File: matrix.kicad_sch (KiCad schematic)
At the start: 189 parts

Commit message: Outline adjustment, footprint cleanup
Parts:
- Stab-225U1, Stab-225U2, Stab-225U3, Stab-275U1, Stab-2U1, Stab-625U1, Stab-7U1: symbol Connector_Generic:Conn_01x01 -> Mechanical:MountingHole
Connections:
- no-connect marks 7 -> 0
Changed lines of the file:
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@@
   (junction (at 261.62 203.2) (diameter 0) (color 0 0 0 0)
   )
-  (no_connect (at 231.14 262.89))
-  (no_connect (at 254 262.89))
-  (no_connect (at 208.28 262.89))
-  (no_connect (at 254 267.97))
-  (no_connect (at 231.14 267.97))
-  (no_connect (at 254 273.05))
-  (no_connect (at 208.28 267.97))
   (wire (pts (xy 307.34 146.05) (xy 307.34 144.78))
     (stroke (width 0) (type default) (color 0 0 0 0))
@@
     (pin "2")
   )
-  (symbol (lib_id "Connector_Generic:Conn_01x01") (at 213.36 262.89 0) (unit 1)
+  (symbol (lib_id "Mechanical:MountingHole") (at 213.36 262.89 0) (unit 1)
     (in_bom yes) (on_board yes)
     (property "Reference" "Stab-625U1" (id 0) (at 215.392 261.8232 0)
@@
       (effects (font (size 1.27 1.27)) hide)
     )
-    (pin "1")
   )
   (symbol (lib_id "MX_Alps_Hybrid:MX-NoLED") (at 97.79 97.79 0) (unit 1)
@@
     (pin "2")
   )
-  (symbol (lib_id "Connector_Generic:Conn_01x01") (at 213.36 267.97 0) (unit 1)
+  (symbol (lib_id "Mechanical:MountingHole") (at 213.36 267.97 0) (unit 1)
     (in_bom yes) (on_board yes)
     (property "Reference" "Stab-7U1" (id 0) (at 215.392 266.9032 0)
@@
       (effects (font (size 1.27 1.27)) hide)
     )
-    (pin "1")
   )
   (symbol (lib_id "MX_Alps_Hybrid:MX-NoLED") (at 229.87 135.89 0) (unit 1)
@@
     (pin "2")
   )
-  (symbol (lib_id "Connector_Generic:Conn_01x01") (at 236.22 267.97 0) (unit 1)
+  (symbol (lib_id "Mechanical:MountingHole") (at 236.22 267.97 0) (unit 1)
     (in_bom yes) (on_board yes)
     (property "Reference" "Stab-225U1" (id 0) (at 238.252 266.9032 0)
@@
       (effects (font (size 1.27 1.27)) hide)
     )
-    (pin "1")
   )
   (symbol (lib_id "MX_Alps_Hybrid:MX-NoLED") (at 163.83 173.99 0) (unit 1)
@@
     (pin "2")
   )
-  (symbol (lib_id "Connector_Generic:Conn_01x01") (at 236.22 262.89 0) (unit 1)
+  (symbol (lib_id "Mechanical:MountingHole") (at 236.22 262.89 0) (unit 1)
     (in_bom yes) (on_board yes)
     (property "Reference" "Stab-2U1" (id 0) (at 238.252 261.8232 0)
@@
       (effects (font (size 1.27 1.27)) hide)
     )
-    (pin "1")
   )
   (symbol (lib_id "MX_Alps_Hybrid:MX-NoLED") (at 97.79 199.39 0) (unit 1)
@@
     (pin "2")
   )
-  (symbol (lib_id "Connector_Generic:Conn_01x01") (at 259.08 267.97 0) (unit 1)
+  (symbol (lib_id "Mechanical:MountingHole") (at 259.08 267.97 0) (unit 1)
     (in_bom yes) (on_board yes)
     (property "Reference" "Stab-225U3" (id 0) (at 261.112 266.9032 0)
@@
       (effects (font (size 1.27 1.27)) hide)
     )
-    (pin "1")
   )
   (symbol (lib_id "MX_Alps_Hybrid:MX-NoLED") (at 163.83 199.39 0) (unit 1)
@@
     (pin "2")
   )
-  (symbol (lib_id "Connector_Generic:Conn_01x01") (at 259.08 262.89 0) (unit 1)
+  (symbol (lib_id "Mechanical:MountingHole") (at 259.08 262.89 0) (unit 1)
     (in_bom yes) (on_board yes)
     (property "Reference" "Stab-225U2" (id 0) (at 261.112 261.8232 0)
@@
       (effects (font (size 1.27 1.27)) hide)
     )
-    (pin "1")
   )
-  (symbol (lib_id "Connector_Generic:Conn_01x01") (at 259.08 273.05 0) (unit 1)
+  (symbol (lib_id "Mechanical:MountingHole") (at 259.08 273.05 0) (unit 1)
     (in_bom yes) (on_board yes)
     (property "Reference" "Stab-275U1" (id 0) (at 261.112 271.9832 0)
@@
       (effects (font (size 1.27 1.27)) hide)
     )
-    (pin "1")
   )
 )

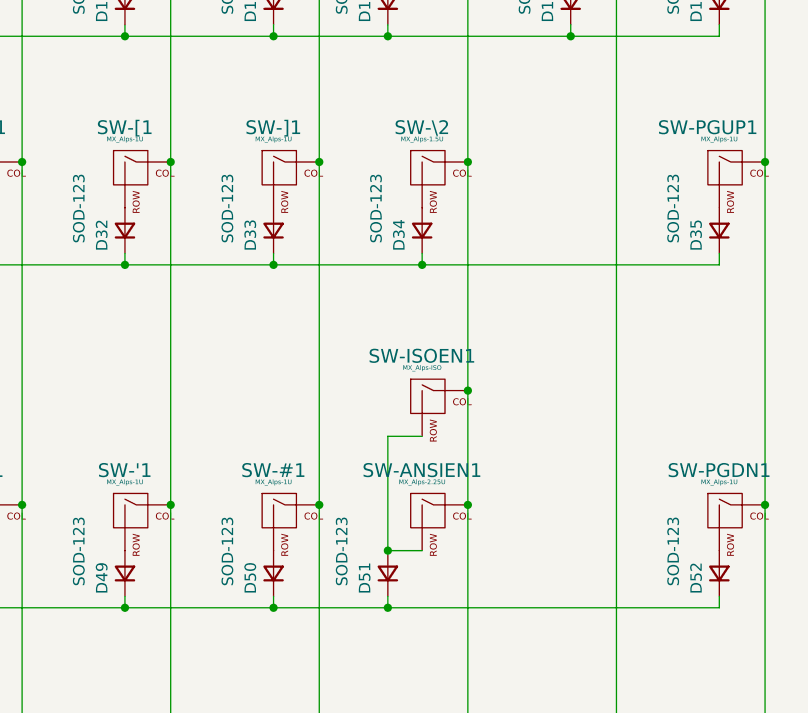
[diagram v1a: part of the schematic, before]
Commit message: Trace cleanup and ISO Enter
Continued trace cleanup for multi-position keys. Added support for three ISO enter orientations - 1.25 vertical and horizontal, and 1.5u vertical.
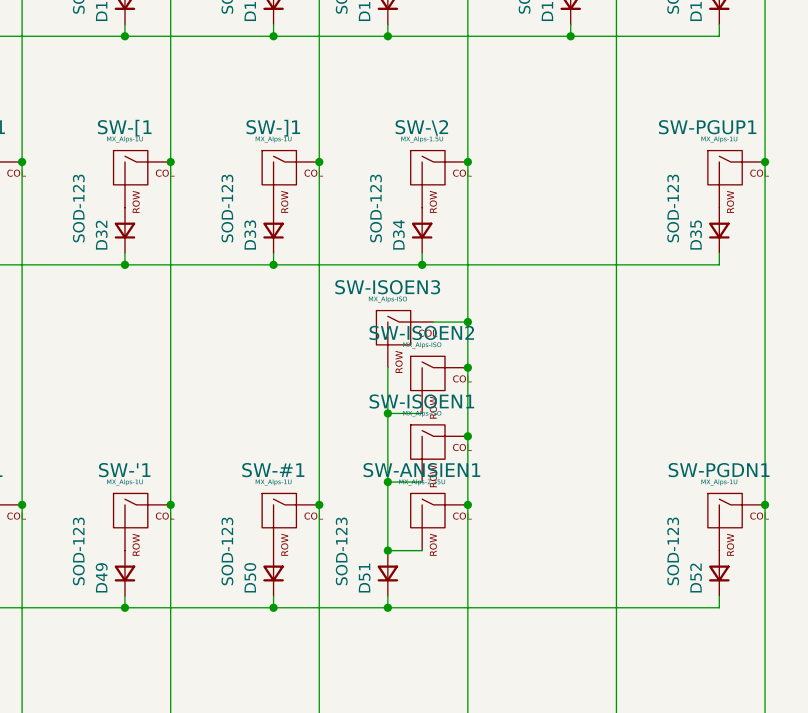
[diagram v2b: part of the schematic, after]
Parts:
- added SW-ISOEN2, SW-ISOEN3: MX_Alps-ISO, Alps_Only:ALPS-1U, symbol MX_Alps_Hybrid:MX-NoLED
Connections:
- net COL15: now also SW-ISOEN2.1 (COL), SW-ISOEN3.1 (COL)
- net at D51.2 (A), SW-ANSIEN1.2 (ROW), SW-ISOEN1.2 (ROW): now also SW-ISOEN2.2 (ROW), SW-ISOEN3.2 (ROW)
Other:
- moved on the sheet: SW-ISOEN1
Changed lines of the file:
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@@
   (junction (at 245.11 203.2) (diameter 0) (color 0 0 0 0)
   )
+  (junction (at 316.23 119.38) (diameter 0) (color 0 0 0 0)
+  )
   (junction (at 96.52 82.55) (diameter 0) (color 0 0 0 0)
   )
@@
   (junction (at 118.11 134.62) (diameter 0) (color 0 0 0 0)
   )
-  (junction (at 316.23 121.92) (diameter 0) (color 0 0 0 0)
+  (junction (at 316.23 127) (diameter 0) (color 0 0 0 0)
   )
   (junction (at 113.03 209.55) (diameter 0) (color 0 0 0 0)
@@
   (junction (at 134.62 96.52) (diameter 0) (color 0 0 0 0)
   )
+  (junction (at 307.34 124.46) (diameter 0) (color 0 0 0 0)
+  )
   (junction (at 311.15 107.95) (diameter 0) (color 0 0 0 0)
   )
@@
   (junction (at 146.05 107.95) (diameter 0) (color 0 0 0 0)
   )
+  (junction (at 316.23 114.3) (diameter 0) (color 0 0 0 0)
+  )
   (junction (at 266.7 134.62) (diameter 0) (color 0 0 0 0)
   )
@@
   (junction (at 96.52 203.2) (diameter 0) (color 0 0 0 0)
   )
+  (junction (at 307.34 132.08) (diameter 0) (color 0 0 0 0)
+  )
   (junction (at 109.22 222.25) (diameter 0) (color 0 0 0 0)
   )
@@
     (stroke (width 0) (type default) (color 0 0 0 0))
   )
-  (wire (pts (xy 307.34 127) (xy 311.15 127))
+  (wire (pts (xy 307.34 132.08) (xy 311.15 132.08))
     (stroke (width 0) (type default) (color 0 0 0 0))
   )
@@
     (stroke (width 0) (type default) (color 0 0 0 0))
   )
-  (wire (pts (xy 307.34 139.7) (xy 307.34 127))
-    (stroke (width 0) (type default) (color 0 0 0 0))
-  )
   (wire (pts (xy 146.05 144.78) (xy 146.05 146.05))
     (stroke (width 0) (type default) (color 0 0 0 0))
@@
     (stroke (width 0) (type default) (color 0 0 0 0))
   )
-  (wire (pts (xy 316.23 121.92) (xy 316.23 134.62))
+  (wire (pts (xy 307.34 119.38) (xy 307.34 124.46))
     (stroke (width 0) (type default) (color 0 0 0 0))
   )
@@
     (stroke (width 0) (type default) (color 0 0 0 0))
   )
+  (wire (pts (xy 307.34 124.46) (xy 311.15 124.46))
+    (stroke (width 0) (type default) (color 0 0 0 0))
+  )
   (wire (pts (xy 327.66 81.28) (xy 327.66 82.55))
     (stroke (width 0) (type default) (color 0 0 0 0))
@@
     (stroke (width 0) (type default) (color 0 0 0 0))
   )
+  (wire (pts (xy 316.23 96.52) (xy 316.23 114.3))
+    (stroke (width 0) (type default) (color 0 0 0 0))
+  )
   (wire (pts (xy 228.6 82.55) (xy 245.11 82.55))
     (stroke (width 0) (type default) (color 0 0 0 0))
@@
     (stroke (width 0) (type default) (color 0 0 0 0))
   )
-  (wire (pts (xy 316.23 96.52) (xy 316.23 121.92))
-    (stroke (width 0) (type default) (color 0 0 0 0))
-  )
   (wire (pts (xy 125.73 222.25) (xy 129.54 222.25))
     (stroke (width 0) (type default) (color 0 0 0 0))
@@
     (stroke (width 0) (type default) (color 0 0 0 0))
   )
+  (wire (pts (xy 312.42 114.3) (xy 316.23 114.3))
+    (stroke (width 0) (type default) (color 0 0 0 0))
+  )
   (wire (pts (xy 212.09 107.95) (xy 228.6 107.95))
     (stroke (width 0) (type default) (color 0 0 0 0))
@@
     (stroke (width 0) (type default) (color 0 0 0 0))
   )
+  (wire (pts (xy 316.23 119.38) (xy 316.23 127))
+    (stroke (width 0) (type default) (color 0 0 0 0))
+  )
   (wire (pts (xy 118.11 217.17) (xy 118.11 198.12))
     (stroke (width 0) (type default) (color 0 0 0 0))
@@
     (stroke (width 0) (type default) (color 0 0 0 0))
   )
+  (wire (pts (xy 307.34 132.08) (xy 307.34 124.46))
+    (stroke (width 0) (type default) (color 0 0 0 0))
+  )
   (wire (pts (xy 80.01 81.28) (xy 80.01 82.55))
     (stroke (width 0) (type default) (color 0 0 0 0))
@@
     (stroke (width 0) (type default) (color 0 0 0 0))
   )
+  (wire (pts (xy 307.34 132.08) (xy 307.34 139.7))
+    (stroke (width 0) (type default) (color 0 0 0 0))
+  )
   (wire (pts (xy 179.07 184.15) (xy 195.58 184.15))
     (stroke (width 0) (type default) (color 0 0 0 0))
@@
     (stroke (width 0) (type default) (color 0 0 0 0))
   )
+  (wire (pts (xy 316.23 127) (xy 316.23 134.62))
+    (stroke (width 0) (type default) (color 0 0 0 0))
+  )
   (wire (pts (xy 101.6 123.19) (xy 101.6 134.62))
     (stroke (width 0) (type default) (color 0 0 0 0))
@@
     (stroke (width 0) (type default) (color 0 0 0 0))
   )
+  (wire (pts (xy 316.23 114.3) (xy 316.23 119.38))
+    (stroke (width 0) (type default) (color 0 0 0 0))
+  )
   (wire (pts (xy 167.64 44.45) (xy 167.64 71.12))
     (stroke (width 0) (type default) (color 0 0 0 0))
@@
     (pin "2")
   )
-  (symbol (lib_id "MX_Alps_Hybrid:MX-NoLED") (at 312.42 123.19 0) (unit 1)
+  (symbol (lib_id "MX_Alps_Hybrid:MX-NoLED") (at 312.42 128.27 0) (unit 1)
     (in_bom yes) (on_board yes)
-    (property "Reference" "SW-ISOEN1" (id 0) (at 311.15 118.11 0)
+    (property "Reference" "SW-ISOEN1" (id 0) (at 311.15 123.19 0)
       (effects (font (size 1.524 1.524)))
     )
-    (property "Value" "MX_Alps-ISO" (id 1) (at 311.15 119.38 0)
+    (property "Value" "MX_Alps-ISO" (id 1) (at 311.15 124.46 0)
       (effects (font (size 0.508 0.508)))
     )
-    (property "Footprint" "Alps_Only:ALPS-ISO-FLIPPED" (id 2) (at 296.545 123.825 0)
+    (property "Footprint" "Alps_Only:ALPS-ISO-FLIPPED" (id 2) (at 296.545 128.905 0)
       (effects (font (size 1.524 1.524)) hide)
     )
-    (property "Datasheet" "" (id 3) (at 296.545 123.825 0)
+    (property "Datasheet" "" (id 3) (at 296.545 128.905 0)
       (effects (font (size 1.524 1.524)) hide)
     )
@@
     )
   )
+  (symbol (lib_id "MX_Alps_Hybrid:MX-NoLED") (at 312.42 120.65 0) (unit 1)
+    (in_bom yes) (on_board yes)
+    (property "Reference" "SW-ISOEN2" (id 0) (at 311.15 115.57 0)
+      (effects (font (size 1.524 1.524)))
+    )
+    (property "Value" "MX_Alps-ISO" (id 1) (at 311.15 116.84 0)
+      (effects (font (size 0.508 0.508)))
+    )
+    (property "Footprint" "Alps_Only:ALPS-1U" (id 2) (at 296.545 121.285 0)
+      (effects (font (size 1.524 1.524)) hide)
+    )
+    (property "Datasheet" "" (id 3) (at 296.545 121.285 0)
+      (effects (font (size 1.524 1.524)) hide)
+    )
+    (pin "1")
+    (pin "2")
+  )
+  (symbol (lib_id "MX_Alps_Hybrid:MX-NoLED") (at 308.61 115.57 0) (unit 1)
+    (in_bom yes) (on_board yes)
+    (property "Reference" "SW-ISOEN3" (id 0) (at 307.34 110.49 0)
+      (effects (font (size 1.524 1.524)))
+    )
+    (property "Value" "MX_Alps-ISO" (id 1) (at 307.34 111.76 0)
+      (effects (font (size 0.508 0.508)))
+    )
+    (property "Footprint" "Alps_Only:ALPS-1U" (id 2) (at 292.735 116.205 0)
+      (effects (font (size 1.524 1.524)) hide)
+    )
+    (property "Datasheet" "" (id 3) (at 292.735 116.205 0)
+      (effects (font (size 1.524 1.524)) hide)
+    )
+    (pin "1")
+    (pin "2")
+  )
 )

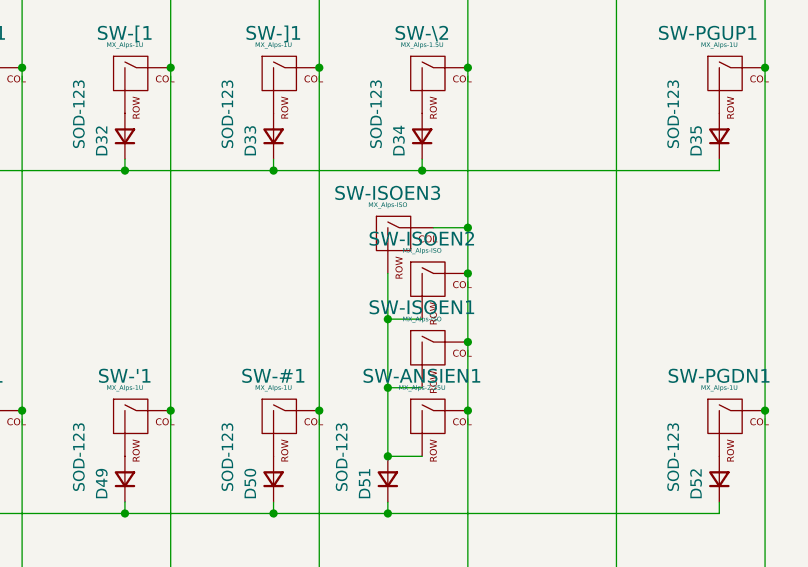
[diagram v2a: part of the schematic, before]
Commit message: Footprint cleanup, add AVR-ISP header footprint
Some cleanup of the bottom row, ISO enter layout, and capslock footprints for more clearance. Addition of the AVR ISP header footprint and mapping to the MCU.
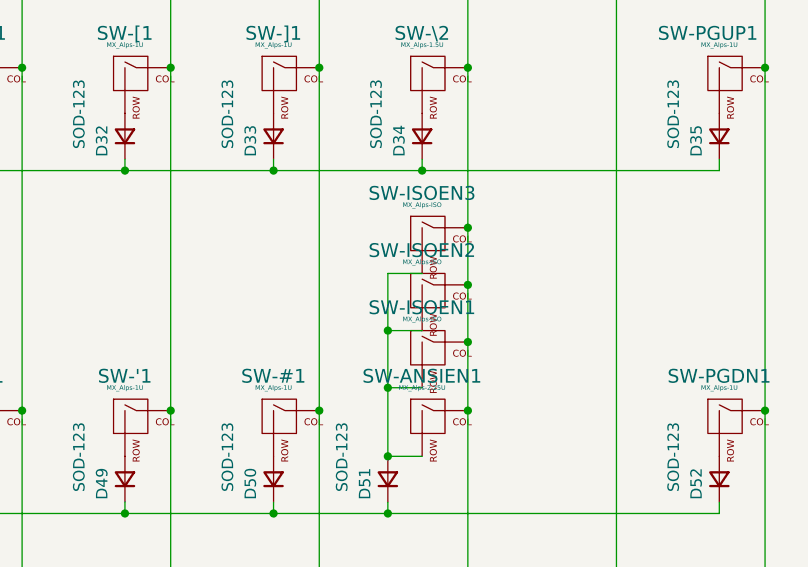
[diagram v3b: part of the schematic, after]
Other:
- moved on the sheet: SW-ISOEN2, SW-ISOEN3
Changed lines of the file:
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@@
   (junction (at 245.11 203.2) (diameter 0) (color 0 0 0 0)
   )
-  (junction (at 316.23 119.38) (diameter 0) (color 0 0 0 0)
-  )
   (junction (at 96.52 82.55) (diameter 0) (color 0 0 0 0)
   )
@@
   (junction (at 134.62 96.52) (diameter 0) (color 0 0 0 0)
   )
-  (junction (at 307.34 124.46) (diameter 0) (color 0 0 0 0)
-  )
   (junction (at 311.15 107.95) (diameter 0) (color 0 0 0 0)
   )
@@
   (junction (at 101.6 160.02) (diameter 0) (color 0 0 0 0)
   )
+  (junction (at 316.23 120.65) (diameter 0) (color 0 0 0 0)
+  )
   (junction (at 228.6 82.55) (diameter 0) (color 0 0 0 0)
   )
@@
   (junction (at 266.7 217.17) (diameter 0) (color 0 0 0 0)
   )
+  (junction (at 307.34 125.73) (diameter 0) (color 0 0 0 0)
+  )
   (junction (at 245.11 209.55) (diameter 0) (color 0 0 0 0)
   )
@@
     (stroke (width 0) (type default) (color 0 0 0 0))
   )
+  (wire (pts (xy 316.23 120.65) (xy 316.23 127))
+    (stroke (width 0) (type default) (color 0 0 0 0))
+  )
   (wire (pts (xy 92.71 184.15) (xy 113.03 184.15))
     (stroke (width 0) (type default) (color 0 0 0 0))
@@
     (stroke (width 0) (type default) (color 0 0 0 0))
   )
-  (wire (pts (xy 307.34 119.38) (xy 307.34 124.46))
-    (stroke (width 0) (type default) (color 0 0 0 0))
-  )
   (wire (pts (xy 179.07 82.55) (xy 195.58 82.55))
     (stroke (width 0) (type default) (color 0 0 0 0))
@@
     (stroke (width 0) (type default) (color 0 0 0 0))
   )
-  (wire (pts (xy 307.34 124.46) (xy 311.15 124.46))
+  (wire (pts (xy 307.34 125.73) (xy 311.15 125.73))
     (stroke (width 0) (type default) (color 0 0 0 0))
   )
@@
     (stroke (width 0) (type default) (color 0 0 0 0))
   )
+  (wire (pts (xy 307.34 119.38) (xy 311.15 119.38))
+    (stroke (width 0) (type default) (color 0 0 0 0))
+  )
   (wire (pts (xy 109.22 234.95) (xy 113.03 234.95))
     (stroke (width 0) (type default) (color 0 0 0 0))
@@
     (stroke (width 0) (type default) (color 0 0 0 0))
   )
-  (wire (pts (xy 312.42 114.3) (xy 316.23 114.3))
-    (stroke (width 0) (type default) (color 0 0 0 0))
-  )
   (wire (pts (xy 212.09 107.95) (xy 228.6 107.95))
     (stroke (width 0) (type default) (color 0 0 0 0))
@@
     (stroke (width 0) (type default) (color 0 0 0 0))
   )
-  (wire (pts (xy 316.23 119.38) (xy 316.23 127))
+  (wire (pts (xy 316.23 114.3) (xy 316.23 120.65))
     (stroke (width 0) (type default) (color 0 0 0 0))
   )
@@
     (stroke (width 0) (type default) (color 0 0 0 0))
   )
+  (wire (pts (xy 307.34 125.73) (xy 307.34 119.38))
+    (stroke (width 0) (type default) (color 0 0 0 0))
+  )
   (wire (pts (xy 274.32 203.2) (xy 278.13 203.2))
     (stroke (width 0) (type default) (color 0 0 0 0))
@@
     (stroke (width 0) (type default) (color 0 0 0 0))
   )
-  (wire (pts (xy 307.34 132.08) (xy 307.34 124.46))
+  (wire (pts (xy 307.34 132.08) (xy 307.34 125.73))
     (stroke (width 0) (type default) (color 0 0 0 0))
   )
@@
     (stroke (width 0) (type default) (color 0 0 0 0))
   )
-  (wire (pts (xy 316.23 114.3) (xy 316.23 119.38))
-    (stroke (width 0) (type default) (color 0 0 0 0))
-  )
   (wire (pts (xy 167.64 44.45) (xy 167.64 71.12))
     (stroke (width 0) (type default) (color 0 0 0 0))
@@
     )
   )
-  (symbol (lib_id "MX_Alps_Hybrid:MX-NoLED") (at 312.42 120.65 0) (unit 1)
+  (symbol (lib_id "MX_Alps_Hybrid:MX-NoLED") (at 312.42 121.92 0) (unit 1)
     (in_bom yes) (on_board yes)
-    (property "Reference" "SW-ISOEN2" (id 0) (at 311.15 115.57 0)
+    (property "Reference" "SW-ISOEN2" (id 0) (at 311.15 116.84 0)
       (effects (font (size 1.524 1.524)))
     )
-    (property "Value" "MX_Alps-ISO" (id 1) (at 311.15 116.84 0)
+    (property "Value" "MX_Alps-ISO" (id 1) (at 311.15 118.11 0)
       (effects (font (size 0.508 0.508)))
     )
-    (property "Footprint" "Alps_Only:ALPS-1U" (id 2) (at 296.545 121.285 0)
+    (property "Footprint" "Alps_Only:ALPS-1U" (id 2) (at 296.545 122.555 0)
       (effects (font (size 1.524 1.524)) hide)
     )
-    (property "Datasheet" "" (id 3) (at 296.545 121.285 0)
+    (property "Datasheet" "" (id 3) (at 296.545 122.555 0)
       (effects (font (size 1.524 1.524)) hide)
     )
@@
     (pin "2")
   )
-  (symbol (lib_id "MX_Alps_Hybrid:MX-NoLED") (at 308.61 115.57 0) (unit 1)
+  (symbol (lib_id "MX_Alps_Hybrid:MX-NoLED") (at 312.42 115.57 0) (unit 1)
     (in_bom yes) (on_board yes)
-    (property "Reference" "SW-ISOEN3" (id 0) (at 307.34 110.49 0)
+    (property "Reference" "SW-ISOEN3" (id 0) (at 311.15 110.49 0)
       (effects (font (size 1.524 1.524)))
     )
-    (property "Value" "MX_Alps-ISO" (id 1) (at 307.34 111.76 0)
+    (property "Value" "MX_Alps-ISO" (id 1) (at 311.15 111.76 0)
       (effects (font (size 0.508 0.508)))
     )
-    (property "Footprint" "Alps_Only:ALPS-1U" (id 2) (at 292.735 116.205 0)
+    (property "Footprint" "Alps_Only:ALPS-1U" (id 2) (at 296.545 116.205 0)
       (effects (font (size 1.524 1.524)) hide)
     )
-    (property "Datasheet" "" (id 3) (at 292.735 116.205 0)
+    (property "Datasheet" "" (id 3) (at 296.545 116.205 0)
       (effects (font (size 1.524 1.524)) hide)
     )
